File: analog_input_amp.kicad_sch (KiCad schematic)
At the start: 30 parts, among them U301 THS4521ID

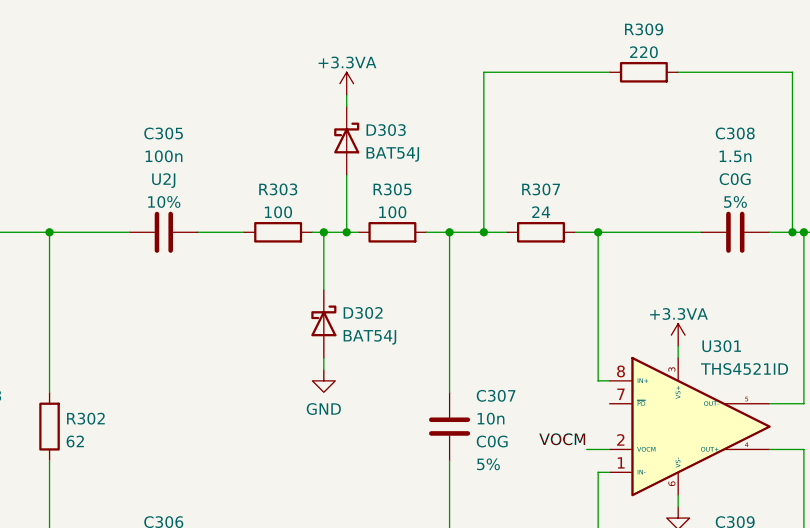
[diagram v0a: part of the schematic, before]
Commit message: Fix: correct BAT54 PN and package - SOD323 not SOD323F
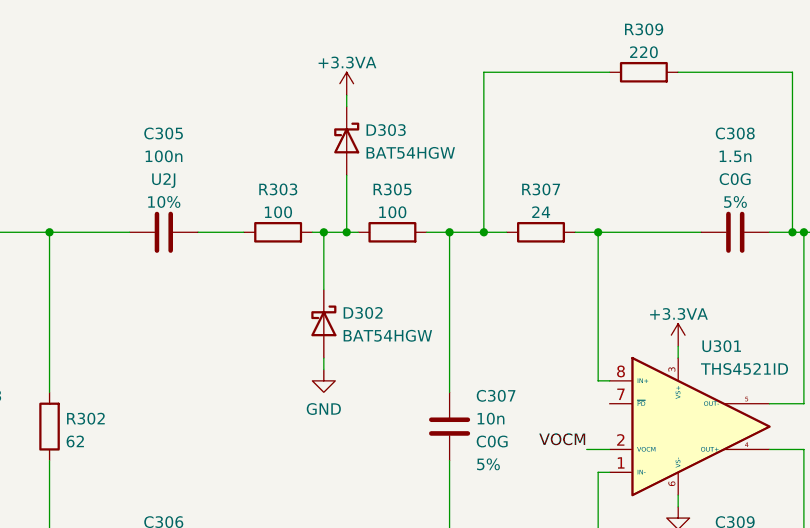
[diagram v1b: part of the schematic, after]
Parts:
- D302, D303: value BAT54J -> BAT54HGW; footprint Diode_SMD:D_SOD-323F -> Diode_SMD:D_SOD-323
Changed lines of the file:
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@@
       (effects (font (size 1.27 1.27)) (justify left))
     )
-    (property "Value" "BAT54J" (id 1) (at 134.112 75.0447 90)
-      (effects (font (size 1.27 1.27)) (justify left))
-    )
-    (property "Footprint" "Diode_SMD:D_SOD-323F" (id 2) (at 127.635 73.66 0)
+    (property "Value" "BAT54HGW" (id 1) (at 134.112 75.0447 90)
+      (effects (font (size 1.27 1.27)) (justify left))
+    )
+    (property "Footprint" "Diode_SMD:D_SOD-323" (id 2) (at 127.635 73.66 0)
       (effects (font (size 1.27 1.27)) hide)
     )
@@
       (effects (font (size 1.27 1.27)) (justify left))
     )
-    (property "Value" "BAT54J" (id 1) (at 136.652 54.7247 90)
-      (effects (font (size 1.27 1.27)) (justify left))
-    )
-    (property "Footprint" "Diode_SMD:D_SOD-323F" (id 2) (at 130.175 53.34 0)
-      (effects (font (size 1.27 1.27)) hide)
-    )
+    (property "Value" "BAT54HGW" (id 1) (at 136.652 54.7247 90)
+      (effects (font (size 1.27 1.27)) (justify left))
+    )
+    (property "Footprint" "Diode_SMD:D_SOD-323" (id 2) (at 130.175 53.34 0)
+      (effects (font (size 1.27 1.27)) hide)
+    )
